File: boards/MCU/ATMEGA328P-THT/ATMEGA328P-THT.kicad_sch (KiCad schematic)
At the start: 3 parts

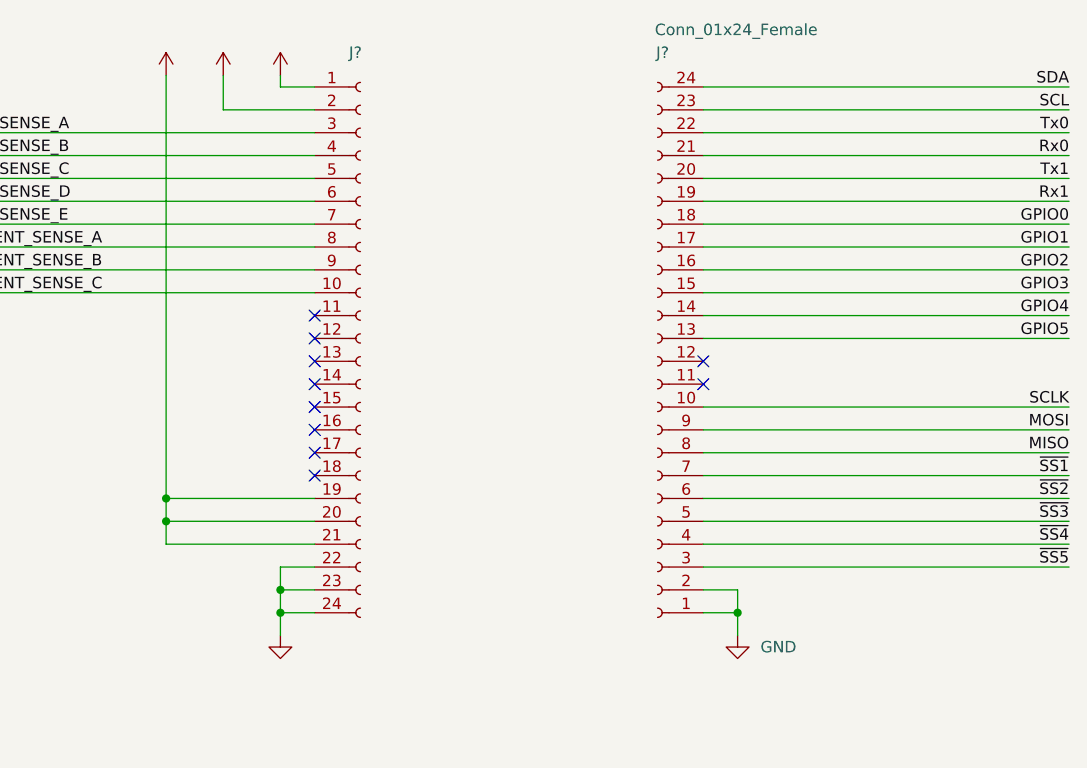
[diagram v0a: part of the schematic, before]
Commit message: Changed from 24 to 22 pin connectors
Signed-off-by: Matthew Nickson <mnickson@sidingsmedia.com>
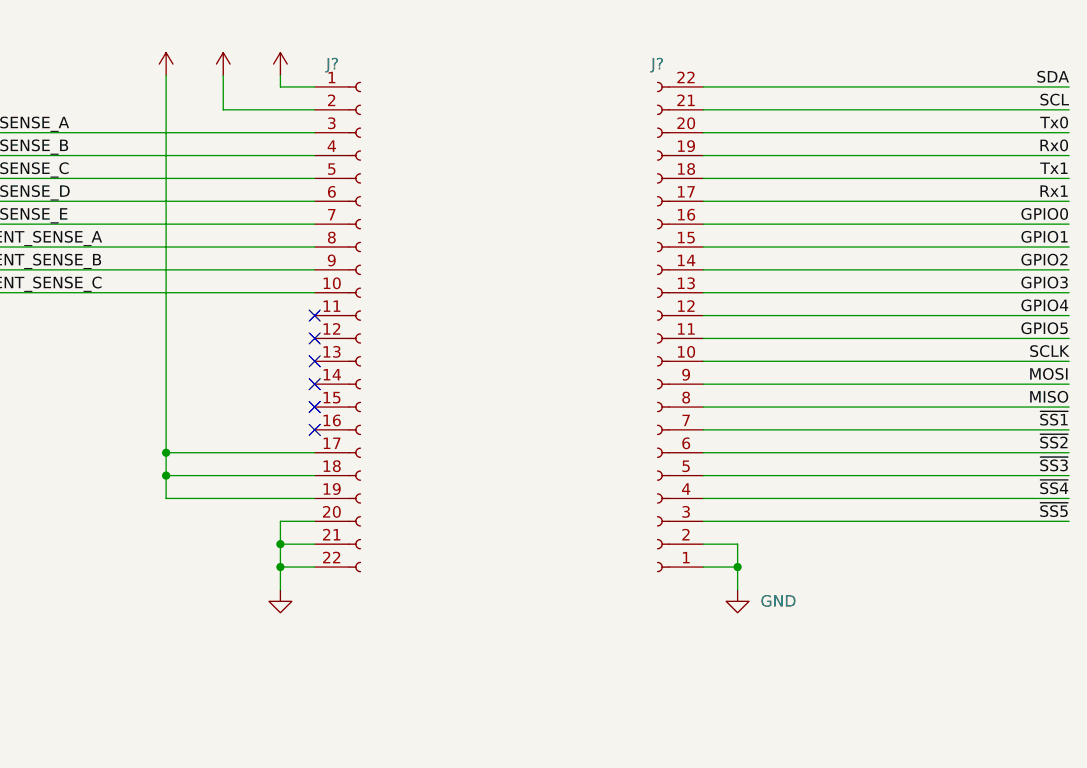
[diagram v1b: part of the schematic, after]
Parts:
- removed J?: Conn_01x24_Female, symbol Connector:Conn_01x24_Female
- removed J?: (no value), symbol Connector:Conn_01x24_Female
- added J? (x2): (no value), symbol Connector:Conn_01x22_Female
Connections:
- net +12V: now also J?.17 (Pin_17), J?.18 (Pin_18), J?.19 (Pin_19)
- net +3V3: now also J?.2 (Pin_2)
- net +5V: now also J?.1 (Pin_1)
- net CURRENT_SENSE_A: now also J?.8 (Pin_8)
- net CURRENT_SENSE_B: now also J?.9 (Pin_9)
- net CURRENT_SENSE_C: now also J?.10 (Pin_10)
- net GND: now also J?.1 (Pin_1), J?.2 (Pin_2), J?.20 (Pin_20), J?.21 (Pin_21), J?.22 (Pin_22)
- net GPIO0: now also J?.16 (Pin_16)
- net GPIO1: now also J?.15 (Pin_15)
- net GPIO2: now also J?.14 (Pin_14)
- net GPIO3: now also J?.13 (Pin_13)
- net GPIO4: now also J?.12 (Pin_12)
- net GPIO5: now also J?.11 (Pin_11)
- net MISO: now also J?.8 (Pin_8)
- net MOSI: now also J?.9 (Pin_9)
- net Rx0: now also J?.19 (Pin_19)
- net Rx1: now also J?.17 (Pin_17)
- net SCL: now also J?.21 (Pin_21)
- net SCLK: now also J?.10 (Pin_10)
- net SDA: now also J?.22 (Pin_22)
- net TEMP_SENSE_A: now also J?.3 (Pin_3)
- net TEMP_SENSE_B: now also J?.4 (Pin_4)
- net TEMP_SENSE_C: now also J?.5 (Pin_5)
- net TEMP_SENSE_D: now also J?.6 (Pin_6)
- net TEMP_SENSE_E: now also J?.7 (Pin_7)
- net Tx0: now also J?.20 (Pin_20)
- net Tx1: now also J?.18 (Pin_18)
- net ~{SS1}: now also J?.7 (Pin_7)
- net ~{SS2}: now also J?.6 (Pin_6)
- net ~{SS3}: now also J?.5 (Pin_5)
- net ~{SS4}: now also J?.4 (Pin_4)
- net ~{SS5}: now also J?.3 (Pin_3)
- no-connect marks 10 -> 6

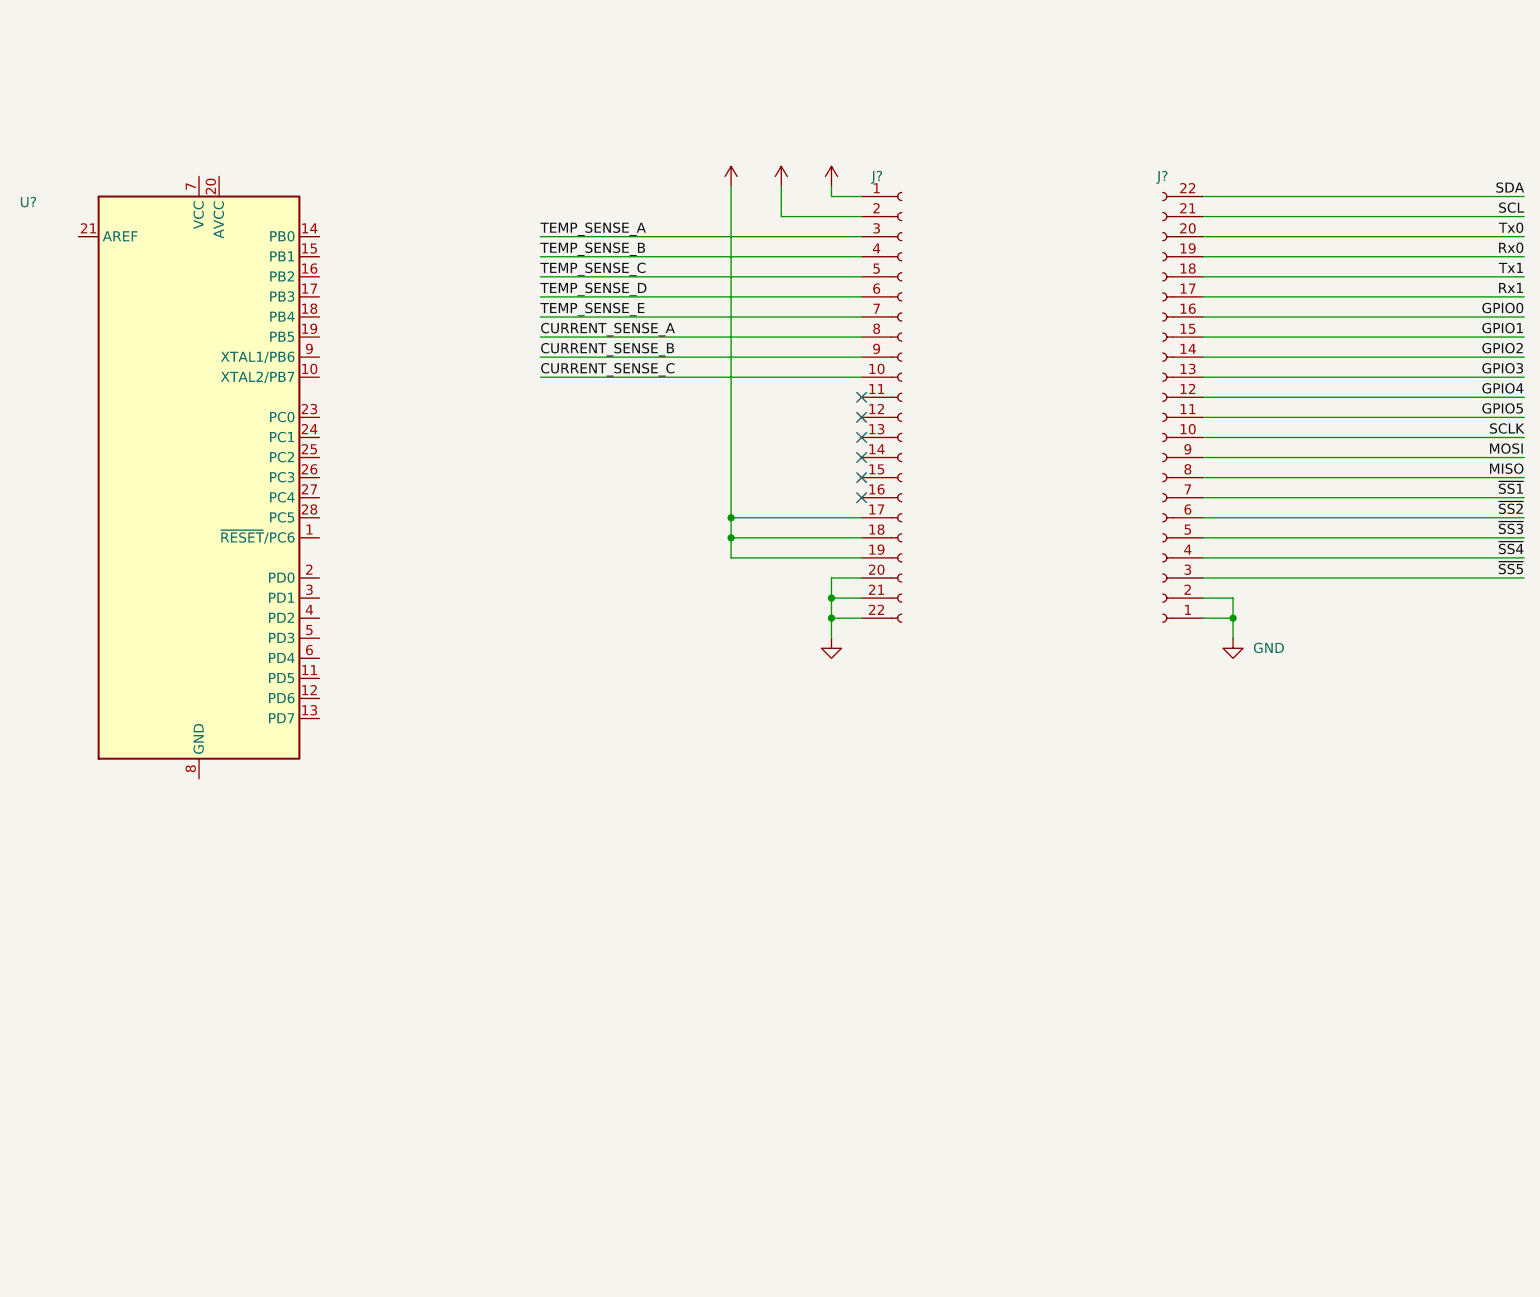
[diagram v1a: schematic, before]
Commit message: Added ATMEGA328P THT MCU board
Signed-off-by: Matthew Nickson <mnickson@sidingsmedia.com>
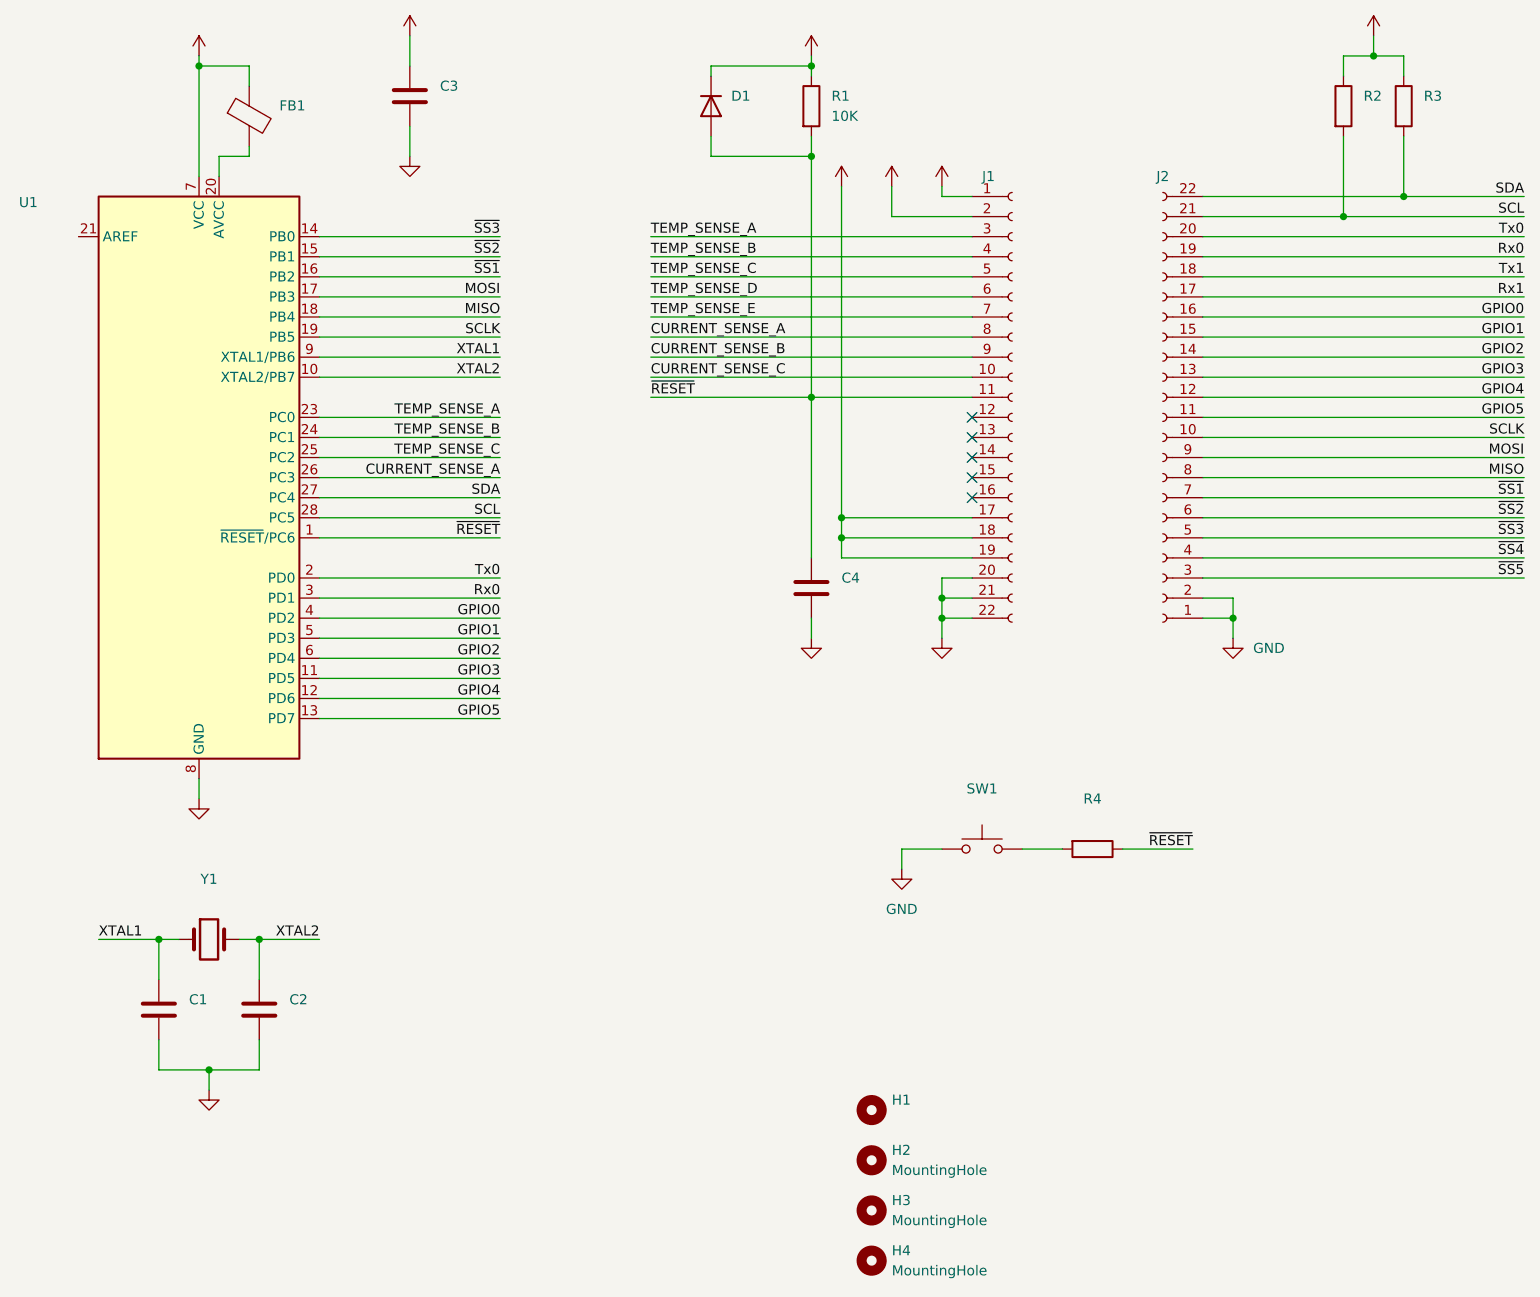
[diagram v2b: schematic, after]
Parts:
- added C1, C2, C3, C4: (no value), symbol Device:C
- added D1: (no value), symbol Device:D
- added FB1: (no value), symbol Device:FerriteBead
- added H1: (no value), symbol Mechanical:MountingHole
- added H2, H3, H4: MountingHole, symbol Mechanical:MountingHole
- added R1: 10K, symbol Device:R
- added R2, R3, R4: (no value), symbol Device:R
- added SW1: (no value), symbol Switch:SW_Push
- added Y1: (no value), symbol Device:Crystal
- gave numbers to parts that had none: 3
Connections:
- net +5V: now also U1.7 (VCC), C3.1, D1.1 (K), FB1.1, R1.1, R2.1, R3.1
- net CURRENT_SENSE_A: now also U1.26 (PC3)
- net GND: now also U1.22 (GND), U1.8 (GND), C1.2, C2.2, C3.2, C4.2, SW1.1
- net GPIO0: now also U1.4 (PD2)
- net GPIO1: now also U1.5 (PD3)
- net GPIO2: now also U1.6 (PD4)
- net GPIO3: now also U1.11 (PD5)
- net GPIO4: now also U1.12 (PD6)
- net GPIO5: now also U1.13 (PD7)
- net MISO: now also U1.18 (PB4)
- net MOSI: now also U1.17 (PB3)
- net Rx0: now also U1.3 (PD1)
- net SCL: now also U1.28 (PC5), R2.2
- net SCLK: now also U1.19 (PB5)
- net SDA: now also U1.27 (PC4), R3.2
- net TEMP_SENSE_A: now also U1.23 (PC0)
- net TEMP_SENSE_B: now also U1.24 (PC1)
- net TEMP_SENSE_C: now also U1.25 (PC2)
- net Tx0: now also U1.2 (PD0)
- net ~{SS1}: now also U1.16 (PB2)
- net ~{SS2}: now also U1.15 (PB1)
- net ~{SS3}: now also U1.14 (PB0)
- net ~{RESET}: now reaches U1.1 (~{RESET}/PC6)
- net ~{RESET}: now also J1.11 (Pin_11), C4.1, D1.2 (A), R1.2, R4.1
- net XTAL2: now reaches U1.10 (XTAL2/PB7)
- net XTAL2: now also C2.1, Y1.2
- net at U1.20 (AVCC): now also FB1.2
- net XTAL1: now reaches U1.9 (XTAL1/PB6)
- net XTAL1: now also C1.1, Y1.1
- new net: R4.2, SW1.2
- no-connect marks 6 -> 5
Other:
- moved on the sheet: J1
